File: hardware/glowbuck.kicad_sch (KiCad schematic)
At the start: 60 parts, among them J101 Conn_02x08_Odd_Even, J102 Conn_01x04_Socket, J103 Conn_01x01_Pin, J104 Conn_01x01_Pin, J105 Conn_01x01_Pin, SW101 SW_Push, SW102 SW_Push, U101 ESP32-S3-WROOM-1, U102 INA181A3, U103 SN74LVC1T45DBV

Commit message: Exchanged shunt resistor
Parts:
- R109: footprint Resistor_SMD:R_0603_1608Metric -> Resistor_SMD:R_0805_2012Metric; ManufacturerNumber WFC06032L000FE66 -> WFC08052L000FE66
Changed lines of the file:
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@@
 			)
 		)
-		(property "Footprint" "Resistor_SMD:R_0603_1608Metric"
+		(property "Footprint" "Resistor_SMD:R_0805_2012Metric"
 			(at 108.712 214.63 90)
 			(effects
@@
 			)
 		)
-		(property "Description" "Resistor"
+		(property "Description" "Current Sense Resistor, 1/2 W"
 			(at 110.49 214.63 0)
 			(effects
@@
 			)
 		)
-		(property "ManufacturerNumber" "WFC06032L000FE66"
+		(property "ManufacturerNumber" "WFC08052L000FE66"
 			(at 110.49 214.63 0)
 			(effects

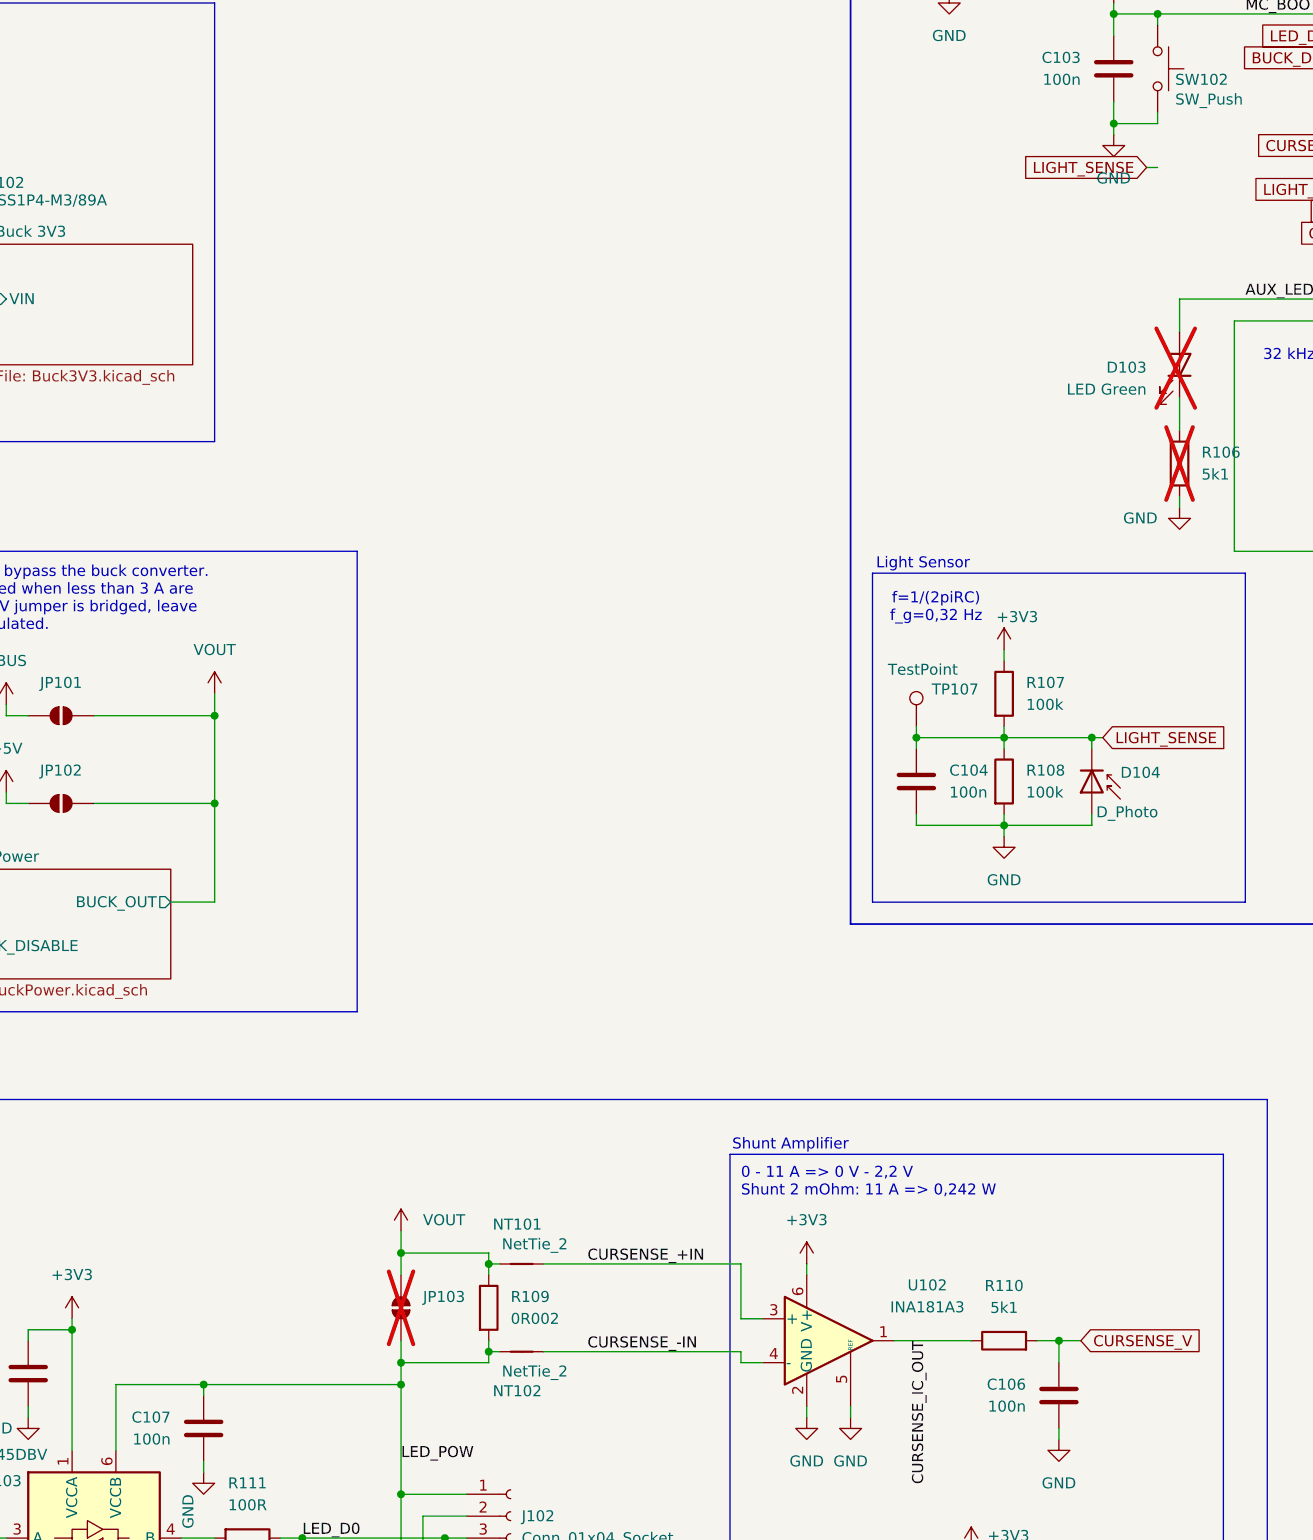
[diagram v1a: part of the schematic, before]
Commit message: Added ManufacturerNumber for every item and fixed bom errors
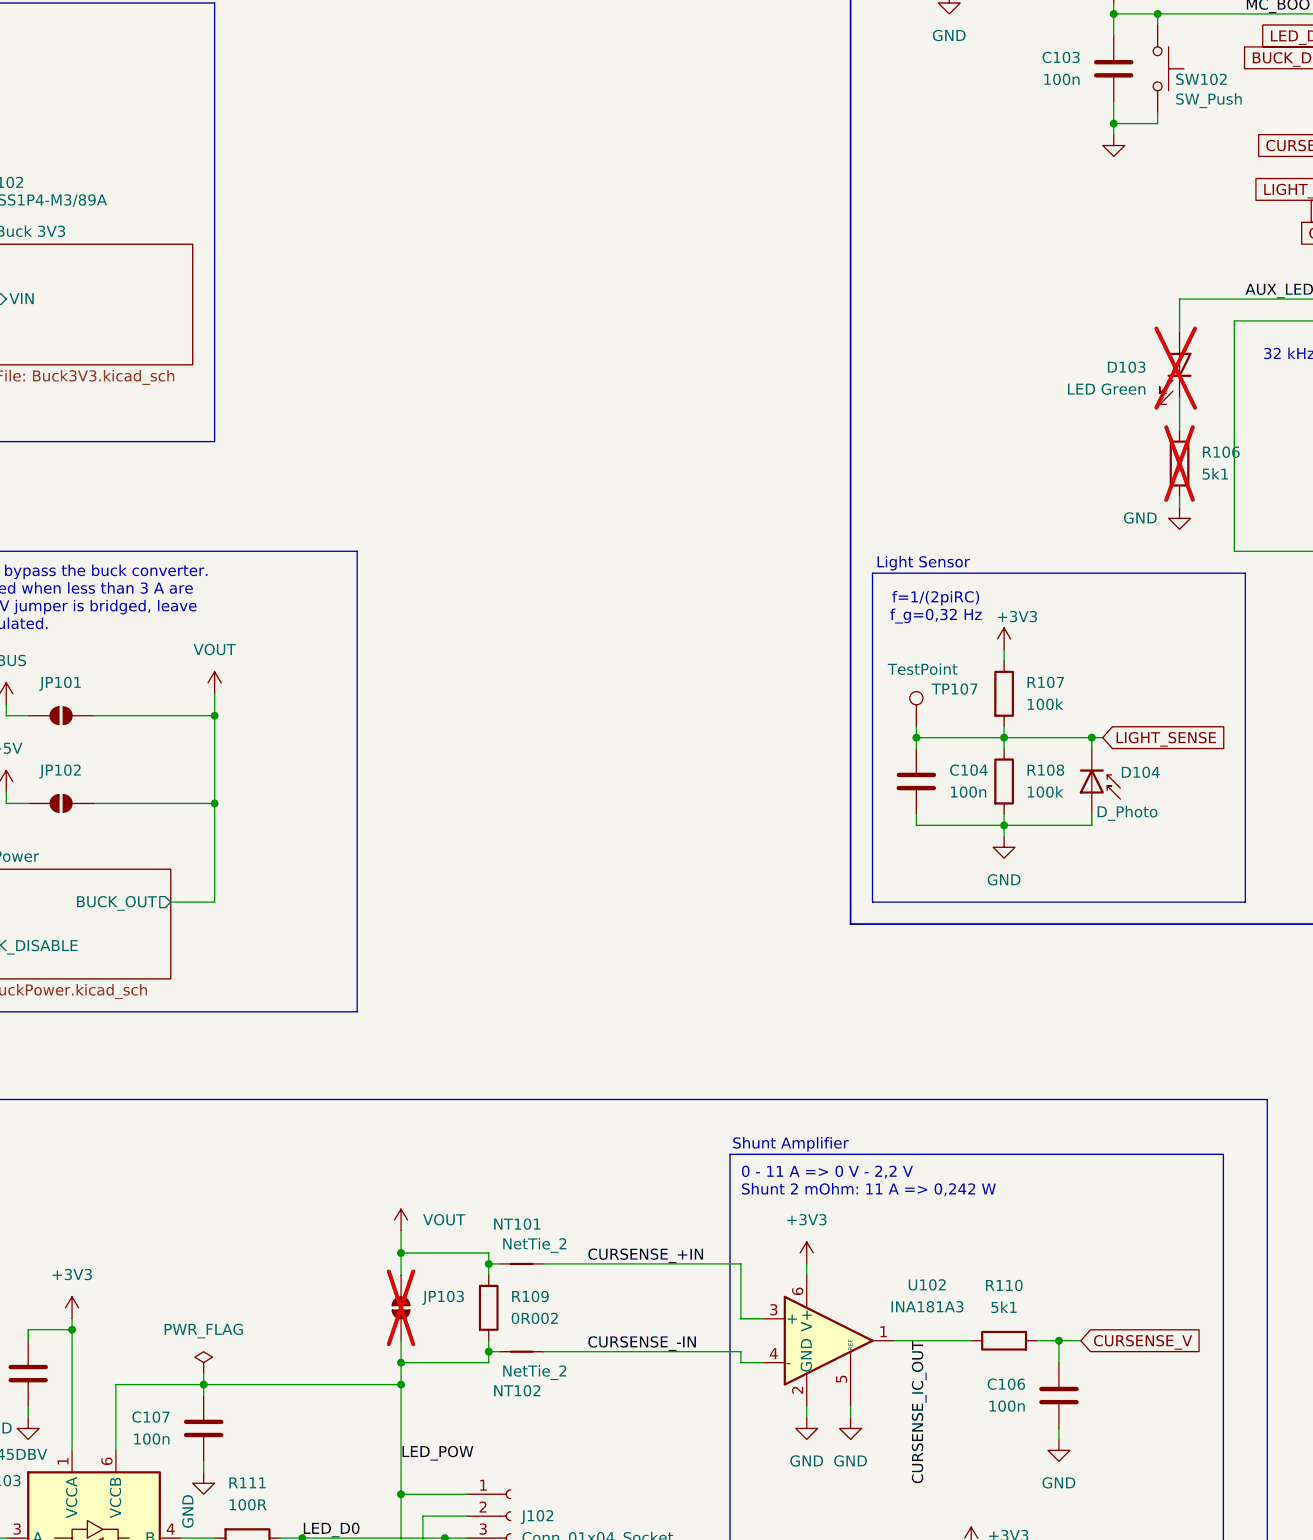
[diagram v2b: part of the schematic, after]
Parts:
- C101: ManufacturerNumber (none) -> CL10A106MA8NRNC
- C102, C103, C104, C105, C106, C107, C108: ManufacturerNumber (none) -> CL10B104KB8WPND
- D101, D102: MouserNumber (none) -> 625-MSS1P4-M3
- D103: ManufacturerNumber (none) -> 150060VS55040
- D104: ManufacturerNumber (none) -> IN-S126BTNPD
- J103, J104, J105: now left out of the parts list
- R101: ManufacturerNumber (none) -> RT0603DRE075K11L; MouserNumber 652-CRT0603FZ1002ELF -> 603-RT0603DRE075K11L
- R102, R104, R105, R106, R110: ManufacturerNumber (none) -> RT0603DRE075K11L; MouserNumber 652-CRT0603FZ1002ELF -> 603-RT0603DRE075K11L; now in the parts list
- R103: ManufacturerNumber (none) -> RC0603FR-130RL
- R107, R108: ManufacturerNumber (none) -> RT0603FRE07100KL
- R109: MouserNumber (none) -> 71-WFC08052L000FE66; now in the parts list
- R111, R112: ManufacturerNumber (none) -> RE0603FRE07100RL; MouserNumber (none) -> 603-RE0603FRE07100RL
- SW101, SW102: ManufacturerNumber (none) -> PTS526SM15SMTR2 LFS
- U101: ManufacturerNumber (none) -> ESP32-S3-WROOM-1-N4
- U102: MouserNumber (none) -> 595-INA181A3IDBVR
- U103: ManufacturerNumber SN74LVC1T45DBV -> SN74LVC1T45DBVRG4; MouserNumber (none) -> 595-74LVC1T45DBVRG4

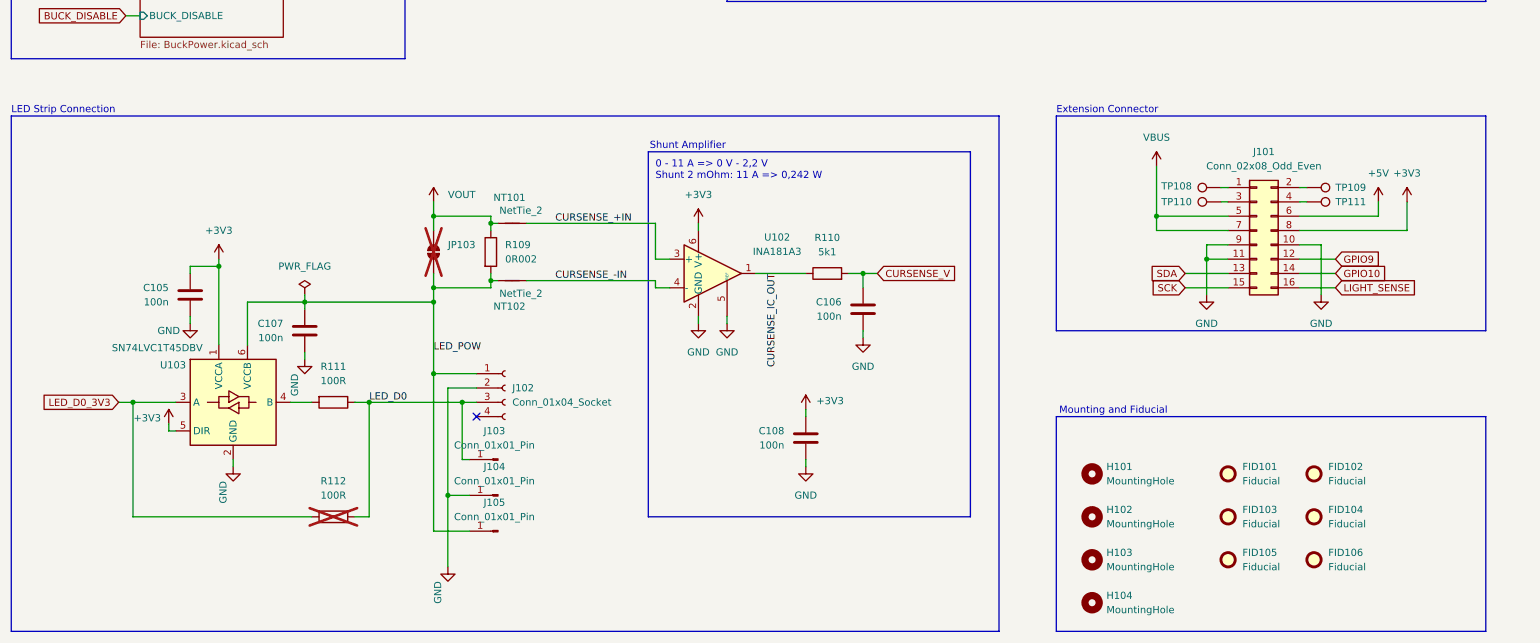
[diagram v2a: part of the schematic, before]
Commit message: Connected VBUS to the free phoenix connector pin
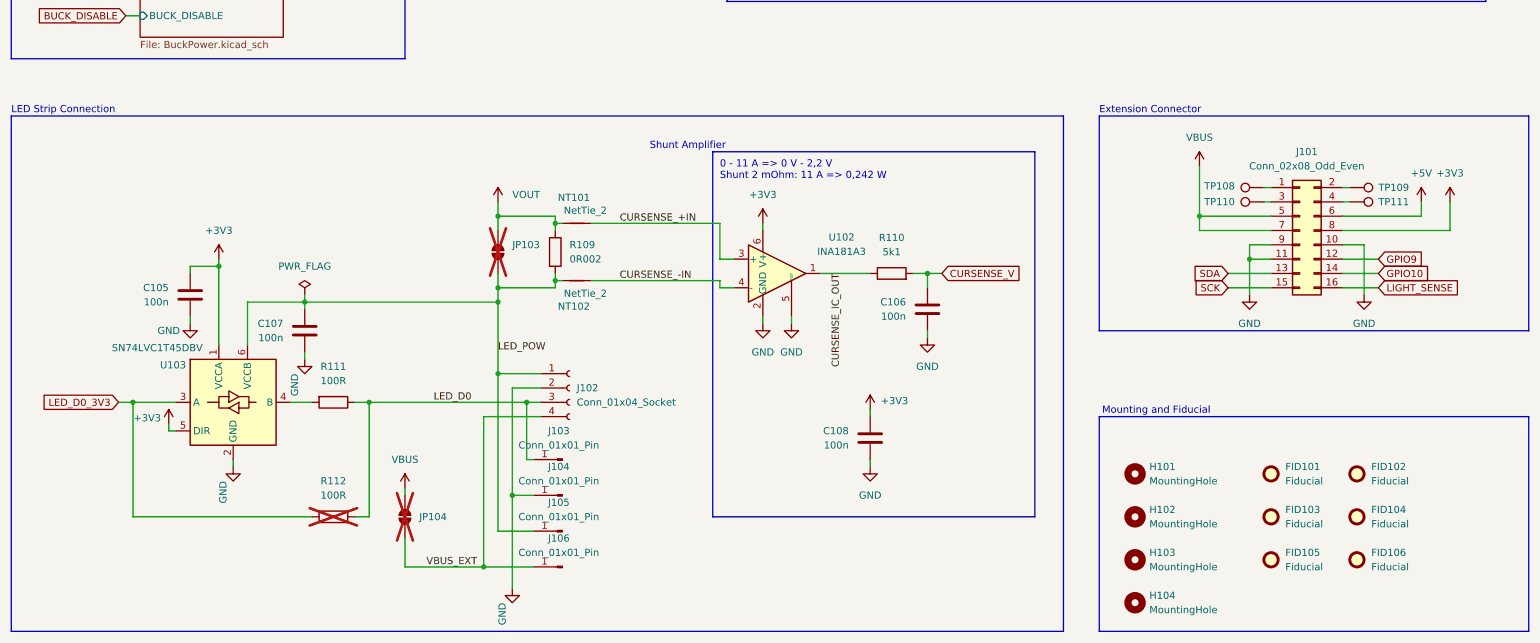
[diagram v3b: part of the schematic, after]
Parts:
- added J106: Conn_01x01_Pin, TestPoint:TestPoint_Pad_3.0x3.0mm, symbol Connector:Conn_01x01_Pin
- added JP104: SolderJumper_2_Open, glowbuck:SolderJumper_Open_HighCurrent, symbol Jumper:SolderJumper_2_Open
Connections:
- net VBUS: now also JP104.2 (B)
- net VBUS_EXT: now reaches J102.4 (Pin_4)
- net VBUS_EXT: now also J106.1 (Pin_1), JP104.1 (A)
- no-connect marks 23 -> 22
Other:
- moved on the sheet: C106, C108, FID101, FID102, FID103, FID104, FID105, FID106, H101, H102, H103, H104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

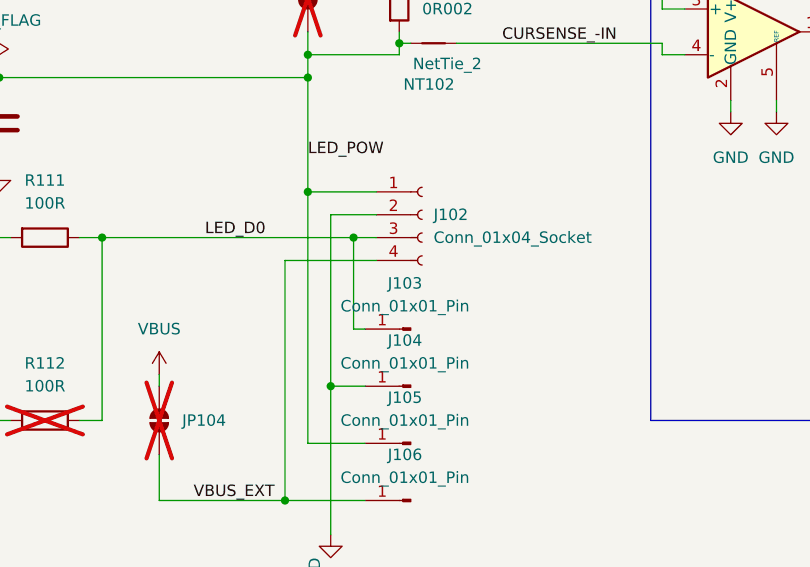
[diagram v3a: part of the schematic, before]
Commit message: Exchanged 5k11 with 5k1 part number
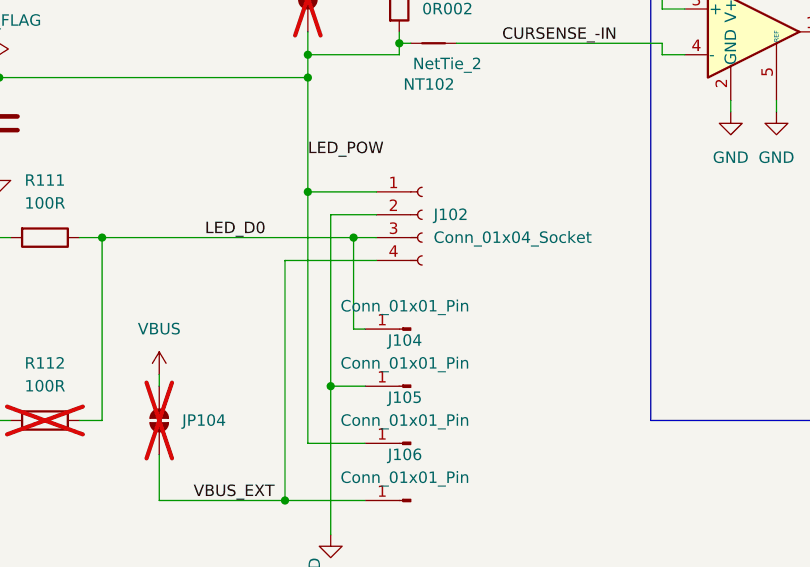
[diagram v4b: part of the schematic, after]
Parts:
- R101, R102, R104, R105, R106, R110: ManufacturerNumber RT0603DRE075K11L -> RC0603FR-105K1L; MouserNumber 603-RT0603DRE075K11L -> 603-RC0603FR-105K1L
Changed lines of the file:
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@@
 			)
 		)
-		(property "MouserNumber" "603-RT0603DRE075K11L"
+		(property "MouserNumber" "603-RC0603FR-105K1L"
 			(at 276.86 69.85 0)
 			(effects
@@
 			)
 		)
-		(property "ManufacturerNumber" "RT0603DRE075K11L"
+		(property "ManufacturerNumber" "RC0603FR-105K1L"
 			(at 276.86 69.85 0)
 			(effects
@@
 			)
 		)
-		(property "MouserNumber" "603-RT0603DRE075K11L"
+		(property "MouserNumber" "603-RC0603FR-105K1L"
 			(at 209.55 120.65 0)
 			(effects
@@
 			)
 		)
-		(property "ManufacturerNumber" "RT0603DRE075K11L"
+		(property "ManufacturerNumber" "RC0603FR-105K1L"
 			(at 209.55 120.65 0)
 			(effects
@@
 					(size 1.27 1.27)
 				)
+				(hide yes)
 			)
 		)
@@
 			)
 		)
-		(property "MouserNumber" "603-RT0603DRE075K11L"
+		(property "MouserNumber" "603-RC0603FR-105K1L"
 			(at 190.5 116.84 0)
 			(effects
@@
 			)
 		)
-		(property "ManufacturerNumber" "RT0603DRE075K11L"
+		(property "ManufacturerNumber" "RC0603FR-105K1L"
 			(at 190.5 116.84 0)
 			(effects
@@
 			)
 		)
-		(property "MouserNumber" "603-RT0603DRE075K11L"
+		(property "MouserNumber" "603-RC0603FR-105K1L"
 			(at 182.88 59.69 0)
 			(effects
@@
 			)
 		)
-		(property "ManufacturerNumber" "RT0603DRE075K11L"
+		(property "ManufacturerNumber" "RC0603FR-105K1L"
 			(at 182.88 59.69 0)
 			(effects
@@
 			)
 		)
-		(property "MouserNumber" "603-RT0603DRE075K11L"
+		(property "MouserNumber" "603-RC0603FR-105K1L"
 			(at 163.83 43.18 0)
 			(effects
@@
 			)
 		)
-		(property "ManufacturerNumber" "RT0603DRE075K11L"
+		(property "ManufacturerNumber" "RC0603FR-105K1L"
 			(at 163.83 43.18 0)
 			(effects
@@
 			)
 		)
-		(property "MouserNumber" "603-RT0603DRE075K11L"
+		(property "MouserNumber" "603-RC0603FR-105K1L"
 			(at 181.61 218.44 0)
 			(effects
@@
 			)
 		)
-		(property "ManufacturerNumber" "RT0603DRE075K11L"
+		(property "ManufacturerNumber" "RC0603FR-105K1L"
 			(at 181.61 218.44 90)
 			(effects

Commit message: Adjusted product numbers and silkscreen for ordernumber
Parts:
- J101: now left out of the parts list
- SW101, SW102: ManufacturerNumber PTS526SM15SMTR2 LFS -> PTS526SM20SMTR21 LFS; MouserNumber 611-PTS526SM15SMTR2L -> 611-PTS526SM20S21LFS
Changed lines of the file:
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@@
 			)
 		)
-		(property "Datasheet" "~"
+		(property "Datasheet" "https://www.ckswitches.com/media/2780/pts526.pdf"
 			(at 193.04 71.12 0)
 			(effects
@@
 			)
 		)
-		(property "MouserNumber" "611-PTS526SM15SMTR2L"
+		(property "MouserNumber" "611-PTS526SM20S21LFS"
 			(at 187.96 71.12 0)
 			(effects
@@
 			)
 		)
-		(property "ManufacturerNumber" "PTS526SM15SMTR2 LFS"
+		(property "ManufacturerNumber" "PTS526SM20SMTR21 LFS"
 			(at 187.96 71.12 90)
 			(effects
@@
 		(unit 1)
 		(exclude_from_sim no)
-		(in_bom yes)
+		(in_bom no)
 		(on_board yes)
 		(dnp no)
@@
 			)
 		)
-		(property "Datasheet" "~"
+		(property "Datasheet" "https://www.ckswitches.com/media/2780/pts526.pdf"
 			(at 173.99 54.61 0)
 			(effects
@@
 			)
 		)
-		(property "MouserNumber" "611-PTS526SM15SMTR2L"
+		(property "MouserNumber" "611-PTS526SM20S21LFS"
 			(at 168.91 54.61 0)
 			(effects
@@
 			)
 		)
-		(property "ManufacturerNumber" "PTS526SM15SMTR2 LFS"
+		(property "ManufacturerNumber" "PTS526SM20SMTR21 LFS"
 			(at 168.91 54.61 90)
 			(effects
